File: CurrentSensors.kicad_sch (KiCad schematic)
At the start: 0 parts

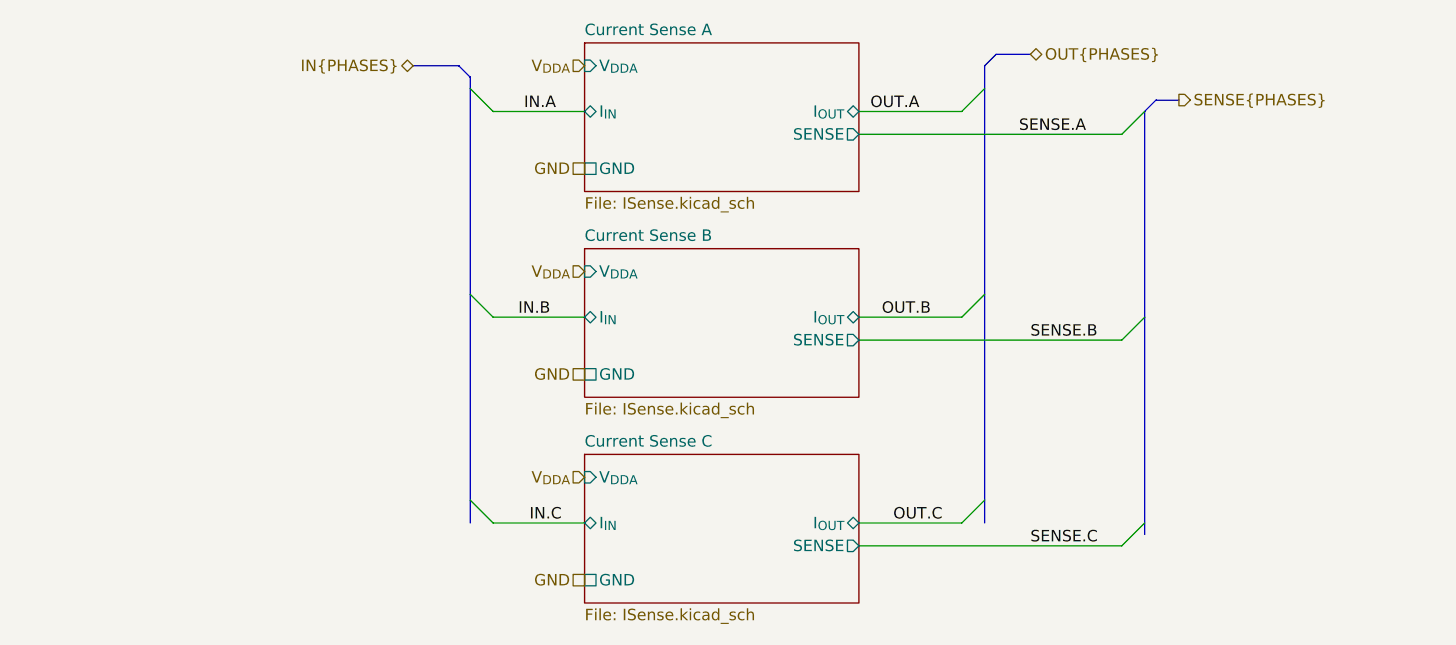
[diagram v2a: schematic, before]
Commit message: added ESD protection
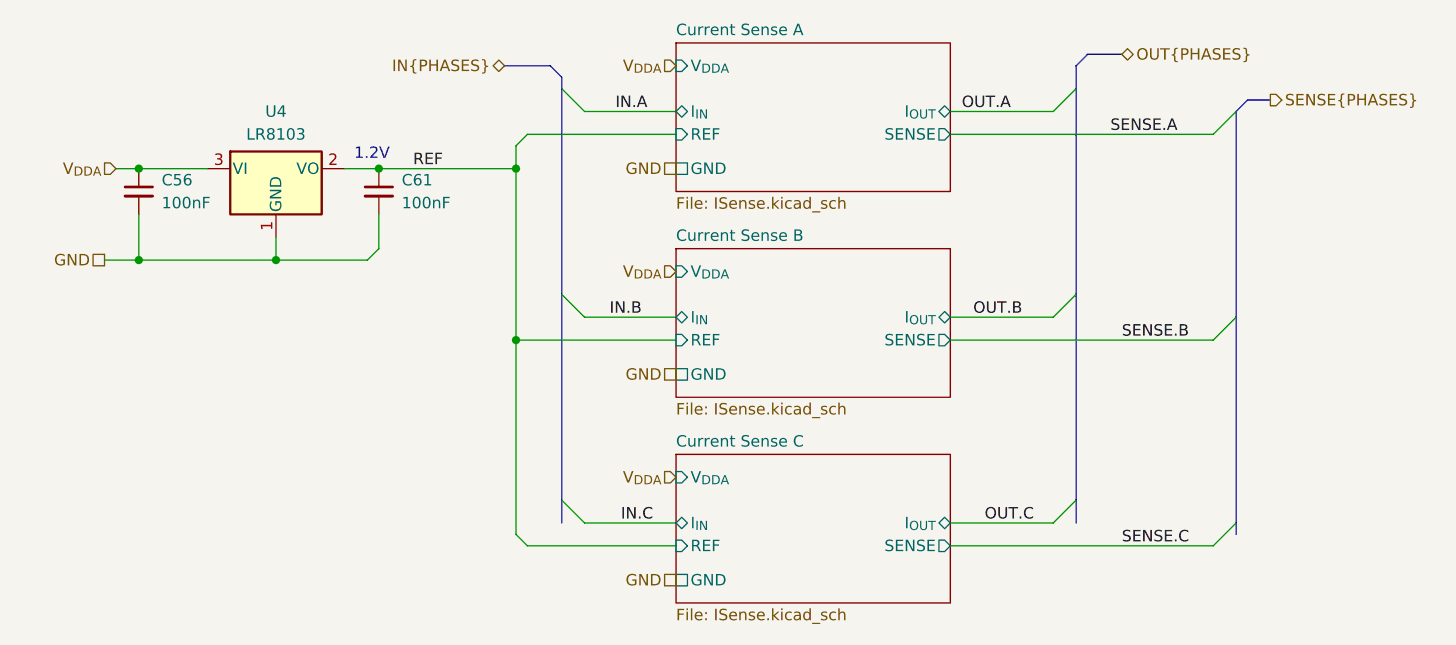
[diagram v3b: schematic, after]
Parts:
- added C56, C61: 100nF, Capacitor_SMD:C_0603_1608Metric, symbol Device:C_Small
- added U4: LR8103, Package_TO_SOT_SMD:SOT-23, symbol Regulator_Linear:MCP1700x-180xxTT
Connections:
- net GND: now also C56.2, C61.2, U4.1 (GND)
- net V_{DDA}: now also C56.1, U4.3 (VI)
- new net REF: C61.1, U4.2 (VO)
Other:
- sheet Current Sense A ports: added REF; removed none
- sheet Current Sense B ports: added REF; removed none
- sheet Current Sense C ports: added REF; removed none
- note added: "1.2V"

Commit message: add context
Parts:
- removed C56, C61: 100nF, Capacitor_SMD:C_0603_1608Metric, symbol Device:C_Small
- removed U4: LR8103, Package_TO_SOT_SMD:SOT-23, symbol Regulator_Linear:MCP1700x-180xxTT
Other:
- sheet Current Sense A ports: added none; removed REF
- sheet Current Sense B ports: added none; removed REF
- sheet Current Sense C ports: added none; removed REF
- note removed: "1.2V"
